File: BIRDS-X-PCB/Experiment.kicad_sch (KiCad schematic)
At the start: 0 parts

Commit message: Add more components
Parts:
- added U4: ~, symbol BIRDS-X_Symbols_Lib:VT01_Radfet
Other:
- note added: "TODO add temp sensors, maybe"
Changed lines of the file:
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@@
 (kicad_sch (version 20230121) (generator eeschema)
   (paper "USLetter")
+  (text "TODO add temp sensors, maybe" (at 100.33 104.14 0)
+    (effects (font (size 1.27 1.27)) (justify left bottom))
+  )
+  (symbol (lib_id "BIRDS-X_Symbols_Lib:VT01_Radfet") (at 105.41 64.77 0) (unit 1)
+    (in_bom yes) (on_board yes) (dnp no) (fields_autoplaced)
+    (property "Reference" "U4" (at 115.57 67.8457 0)
+      (effects (font (size 1.27 1.27)) (justify left))
+    )
+    (property "Value" "~" (at 105.41 64.77 0)
+      (effects (font (size 1.27 1.27)))
+    )
+    (property "Footprint" "" (at 105.41 64.77 0)
+      (effects (font (size 1.27 1.27)) hide)
+    )
+    (property "Datasheet" "" (at 105.41 64.77 0)
+      (effects (font (size 1.27 1.27)) hide)
+    )
+    (pin "1")
+    (pin "2")
+    (pin "3")
+    (pin "4")
+    (pin "5")
+    (pin "6")
+    (instances
+      (project "BIRDS-X-PCB"
+        (path "/c2796b15-795a-4d6e-ad4b-0ba87ded4bc9/adc73a10-1d27-484e-8ce9-d638694b8e29"
+          (reference "U4") (unit 1)
+        )
+      )
+    )
+  )
 )

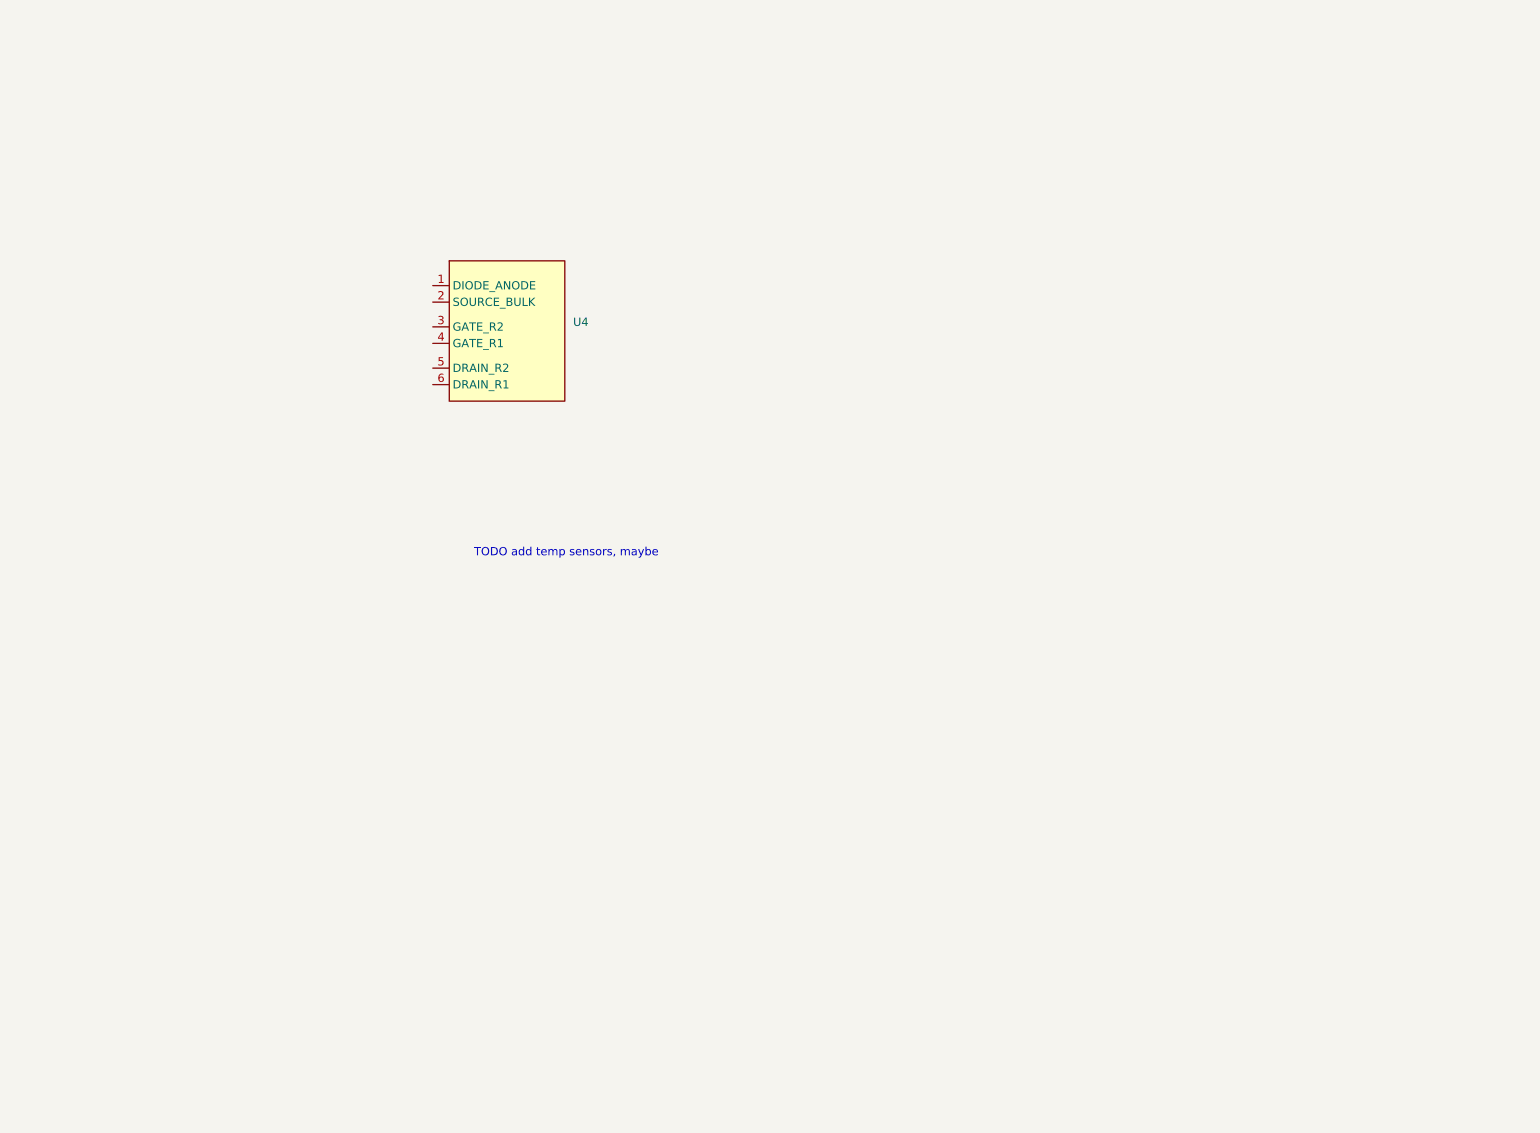
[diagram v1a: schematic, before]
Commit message: Add flash, temperature sensor, etc.
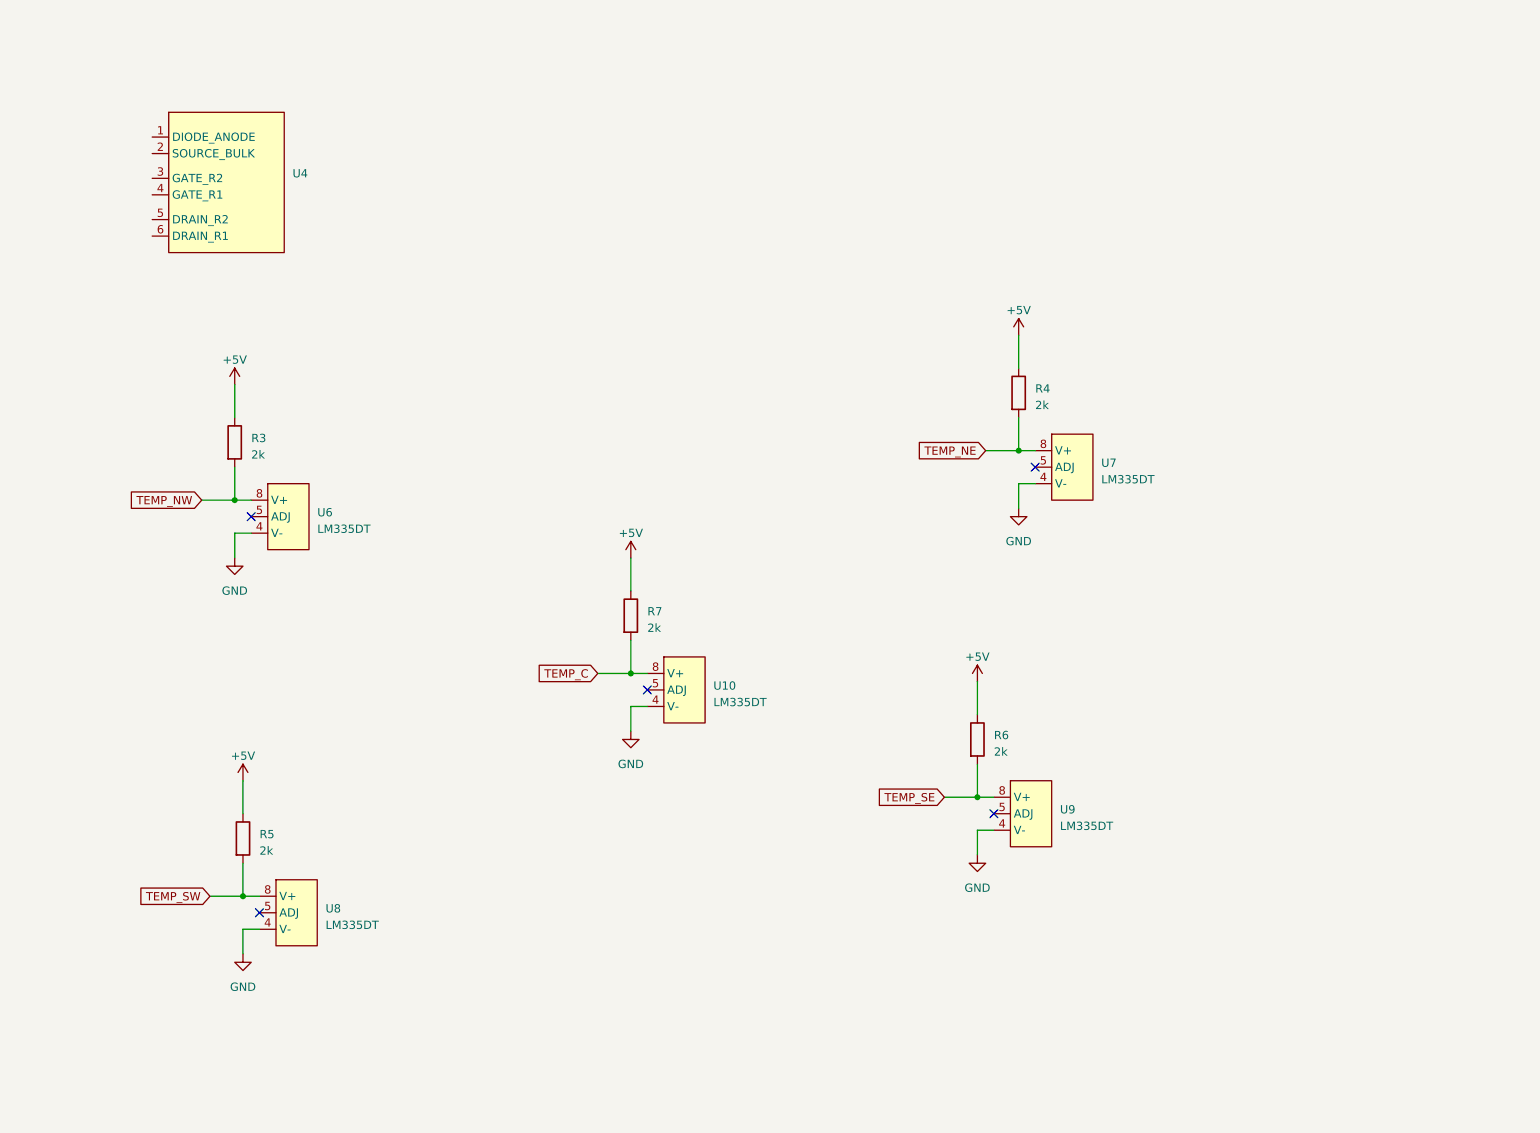
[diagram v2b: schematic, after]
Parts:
- added R3, R4, R5, R6, R7: 2k, symbol Device:R
- added U10, U6, U7, U8, U9: LM335DT, Package_SO:SOIC-8_3.9x4.9mm_P1.27mm, symbol BIRDS-X_Symbols_Lib:LM335DT
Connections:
- new net +5V: R3.1, R4.1, R5.1, R6.1, R7.1
- new net GND: U10.4 (V-), U6.4 (V-), U7.4 (V-), U8.4 (V-), U9.4 (V-)
- new net TEMP_C: R7.2, U10.8 (V+)
- new net TEMP_NE: R4.2, U7.8 (V+)
- new net TEMP_NW: R3.2, U6.8 (V+)
- new net TEMP_SE: R6.2, U9.8 (V+)
- new net TEMP_SW: R5.2, U8.8 (V+)
- no-connect marks 0 -> 5
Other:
- note removed: "TODO add temp sensors, maybe"
- moved on the sheet: U4

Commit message: Add BOM and footprints
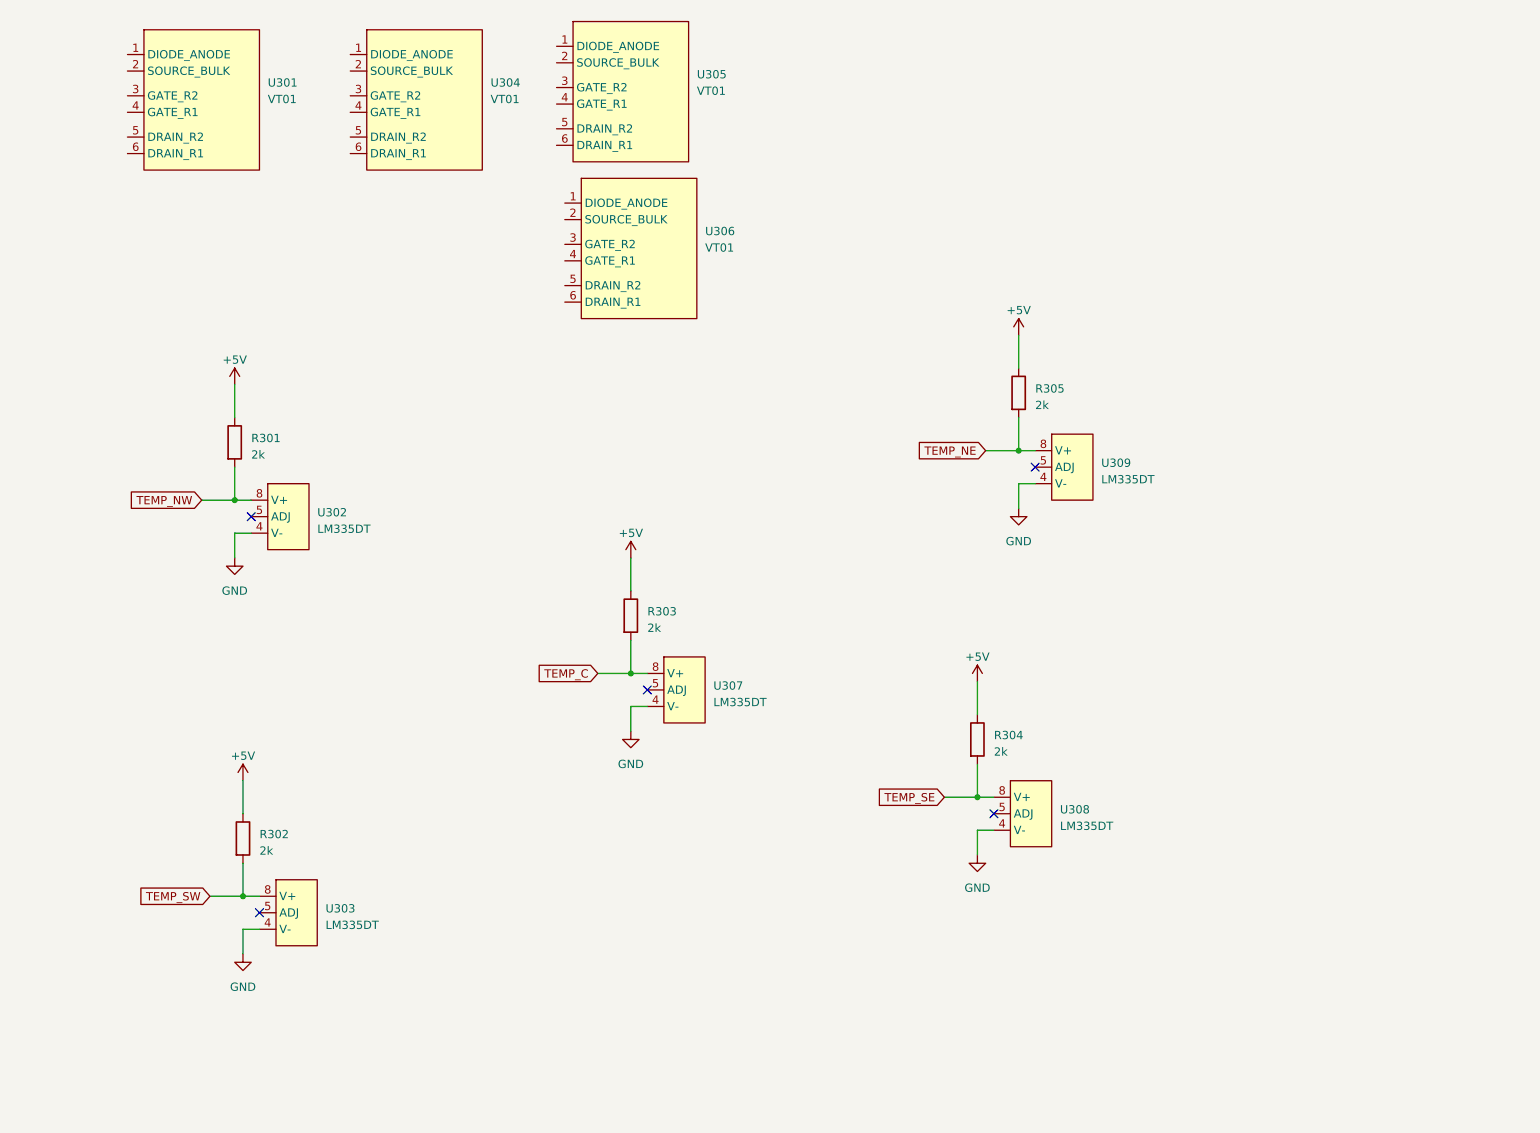
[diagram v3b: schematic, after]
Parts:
- removed U4: ~, symbol BIRDS-X_Symbols_Lib:VT01_Radfet
- added U301, U304, U305, U306: VT01, symbol BIRDS-X_Symbols_Lib:VT01_Radfet
- R301: renamed from R3; footprint (none) -> Resistor_SMD:R_1206_3216Metric_Pad1.30x1.75mm_HandSolder
- R302: renamed from R5; footprint (none) -> Resistor_SMD:R_1206_3216Metric_Pad1.30x1.75mm_HandSolder
- R303: renamed from R7; footprint (none) -> Resistor_SMD:R_1206_3216Metric_Pad1.30x1.75mm_HandSolder
- R304: renamed from R6; footprint (none) -> Resistor_SMD:R_1206_3216Metric_Pad1.30x1.75mm_HandSolder
- R305: renamed from R4; footprint (none) -> Resistor_SMD:R_1206_3216Metric_Pad1.30x1.75mm_HandSolder
- renumbered U6 to U302, U8 to U303, U10 to U307, U9 to U308, U7 to U309

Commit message: Added current source circuitry for RADFET Readout
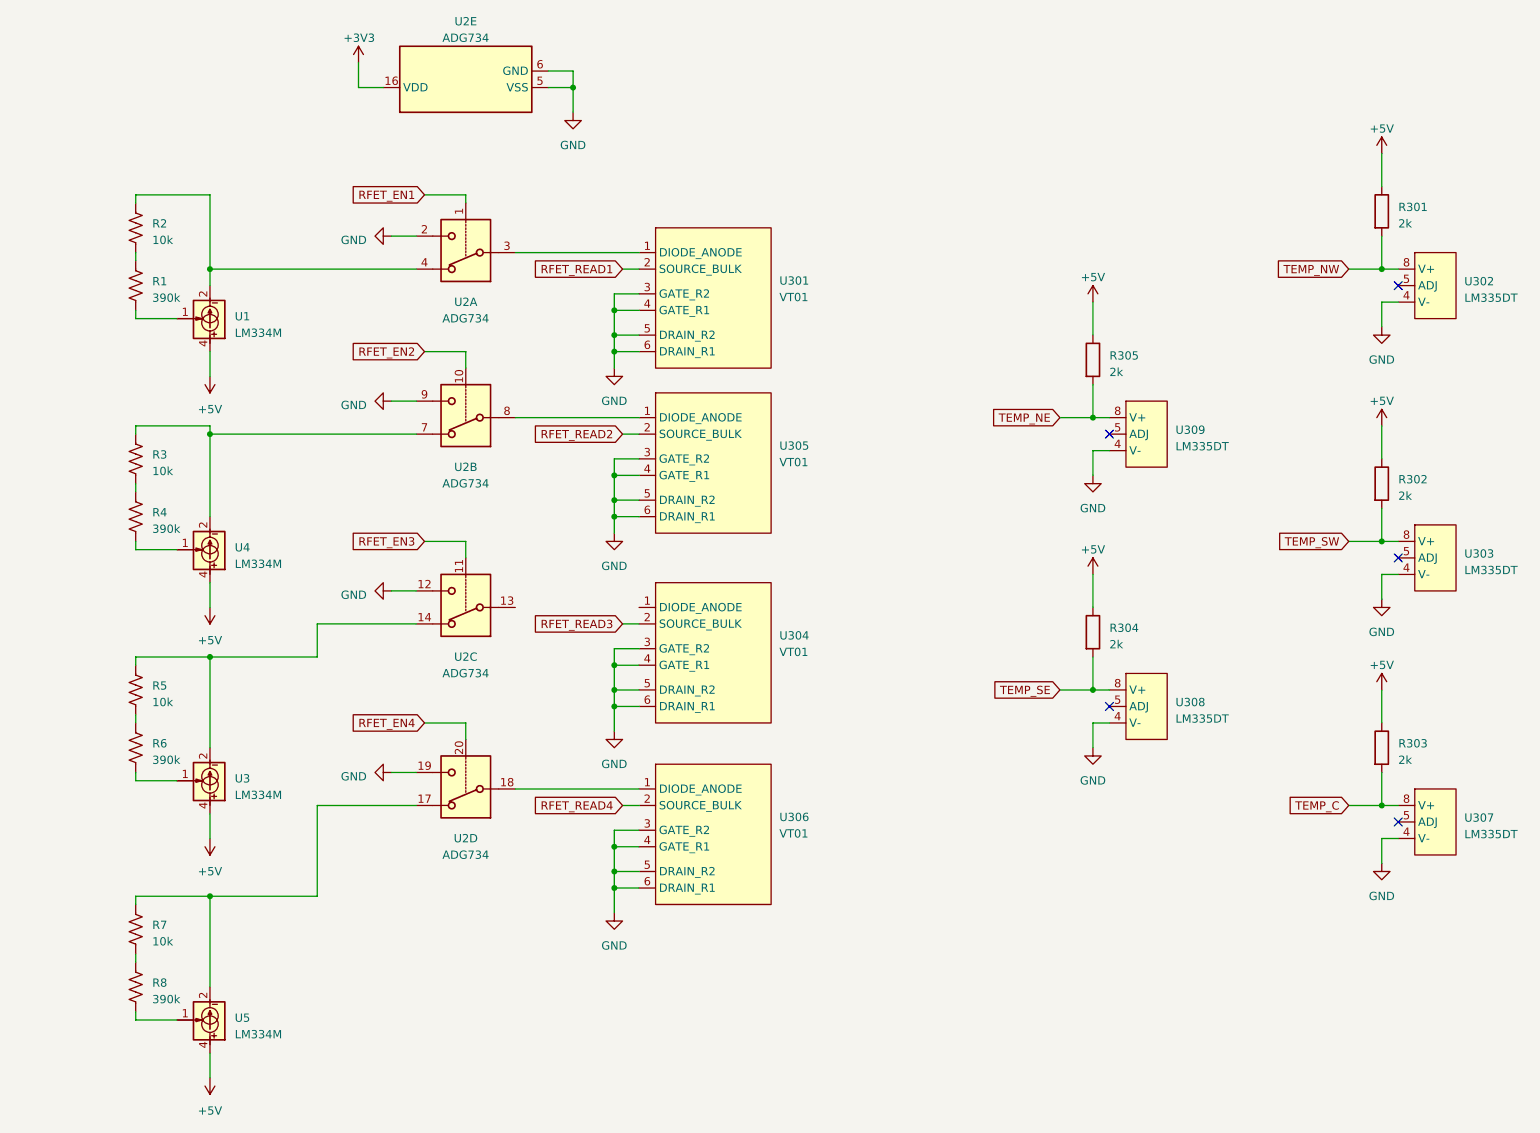
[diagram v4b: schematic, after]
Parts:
- added R1, R4, R6, R8: 390k, Resistor_SMD:R_1206_3216Metric, symbol Device:R_US
- added R2, R3, R5, R7: 10k, Resistor_SMD:R_1206_3216Metric, symbol Device:R_US
- added U1, U3, U4, U5: LM334M, Package_SO:SOIC-8_3.9x4.9mm_P1.27mm, symbol Reference_Current:LM334M
- added U2: ADG734, Package_SO:TSSOP-20_4.4x6.5mm_P0.65mm, symbol Analog_Switch:ADG734
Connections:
- net +5V: now also U1.4, U3.4, U4.4, U5.4
- net GND: now also U301.3 (GATE_R2), U301.4 (GATE_R1), U301.5 (DRAIN_R2), U301.6 (DRAIN_R1), U304.3 (GATE_R2), U304.4 (GATE_R1), U304.5 (DRAIN_R2), U304.6 (DRAIN_R1), U305.3 (GATE_R2), U305.4 (GATE_R1), U305.5 (DRAIN_R2), U305.6 (DRAIN_R1), U306.3 (GATE_R2), U306.4 (GATE_R1), U306.5 (DRAIN_R2), U306.6 (DRAIN_R1), U2.12, U2.19, U2.2, U2.5 (VSS), U2.6 (GND), U2.9
- net at U305.1 (DIODE_ANODE): now also U2.8
- net RFET_READ2: now reaches U305.2 (SOURCE_BULK)
- net at U306.1 (DIODE_ANODE): now also U2.18
- net RFET_READ4: now reaches U306.2 (SOURCE_BULK)
- net RFET_READ3: now reaches U304.2 (SOURCE_BULK)
- net at U301.1 (DIODE_ANODE): now also U2.3
- net RFET_READ1: now reaches U301.2 (SOURCE_BULK)
- new net: R7.2, R8.1
- new net: R8.2, U5.1
- new net: R3.2, R4.1
- new net: R4.2, U4.1
- new net: R1.2, U1.1
- new net: R2.1, U1.2, U1.3, U1.6, U1.7, U2.4
- new net: R5.1, U2.14, U3.2, U3.3, U3.6, U3.7
- new net: R1.1, R2.2
- new net: R6.2, U3.1
- new net: R7.1, U2.17, U5.2, U5.3, U5.6, U5.7
- new net: R3.1, U2.7, U4.2, U4.3, U4.6, U4.7
- new net: R5.2, R6.1
- new net +3V3: U2.16 (VDD)
- new net RFET_EN1: U2.1
- new net RFET_EN2: U2.10
- new net RFET_EN3: U2.11
- new net RFET_EN4: U2.20
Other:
- moved on the sheet: R301, R302, R303, R304, R305, U301, U302, U303, U304, U305, U306, U307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
